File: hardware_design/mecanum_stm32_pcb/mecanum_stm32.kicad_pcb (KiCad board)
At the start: 2 copper layers, 90 x 64 mm, 113 parts, among them J1 BAT 7.4~12.6V, J10 MOTOR A, J11 MOTOR B, J12 MOTOR C, J13 MOTOR D, J2 USB Mini-B, J3 SWD, J4 I2C (MPU6050), J5 SPI IMU, Q1 AO4407A, SW1 RESET, SW2 BOOT0, U1 STM32F405RGT6, U10 DRV8874PWPR, U11 DRV8874PWPR, U12 DRV8874PWPR, U13 DRV8874PWPR, U2 TPS542025 (5V), U3 AMS1117-3.3, U4 CH340C, U5 ADuM1201ARZ, Y1 8MHz 3225 12pF

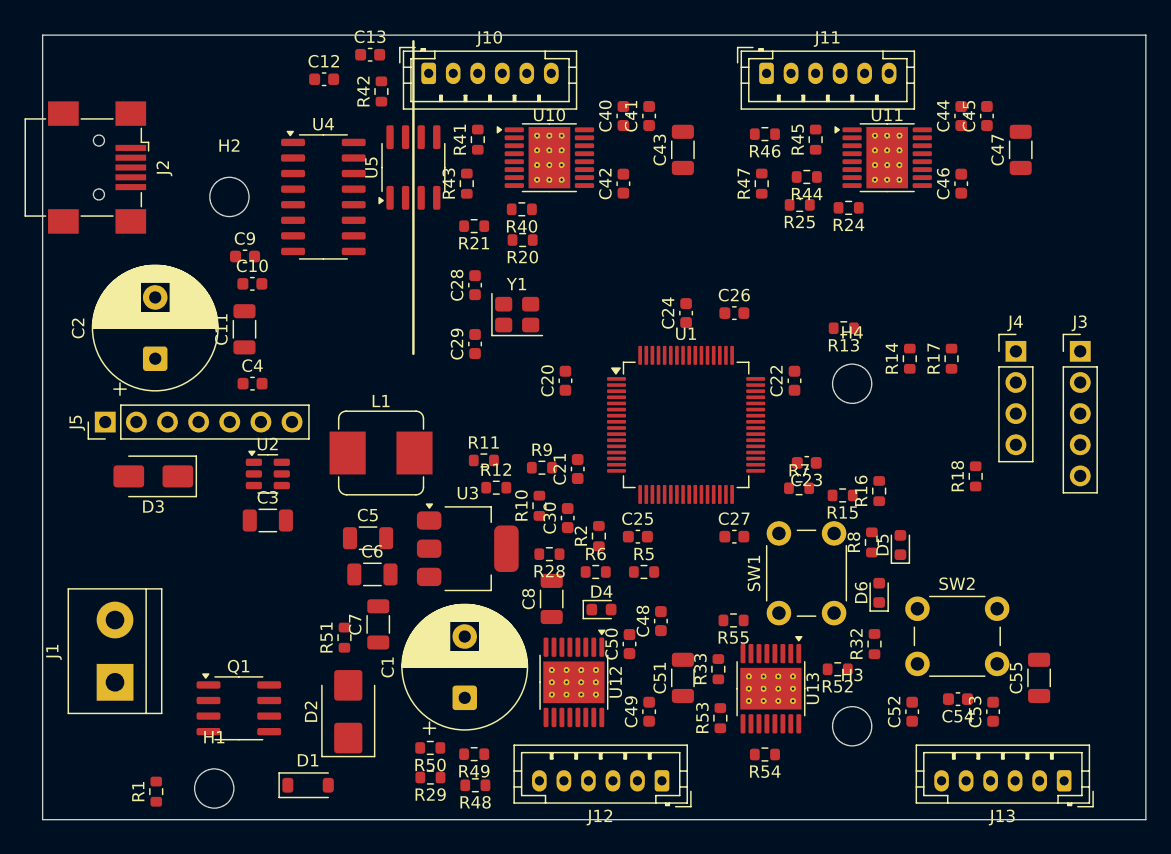
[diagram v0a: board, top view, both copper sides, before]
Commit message: STM32 주행보드 자동배선 완료: 미연결 0·DRC 오류 0, DSN/SES 변환 직접 구현
- route.py: KiCad 9.0.4 ExportSpecctraDSN이 헤드리스에서 멈춰 DSN 쓰기·SES 읽기를 직접 구현,
  Freerouting 2.5.0 연결. 핀에 들어가는 굵기로 배선 후 간격 되는 구간만 0.8/0.6mm로 굵히기,
  양면 GND 동박(USB 칸 GNDU 분리), 고정구멍 둘레 Ø6.5 동박 금지(나사머리가 GNDU를 잇지 않게)
- 넷클래스: Power/Motor/Supply/Default(0.18/0.15mm), 방열 스포크 최소 1
- gen_pcb.py: Mini-B 0.12mm 안쪽, 부품번호 글자 0.8mm
- DRC: 오류 0, 미연결 0, 실크 경고 69

Co-Authored-By: Claude Opus 5.5 <noreply@anthropic.com>
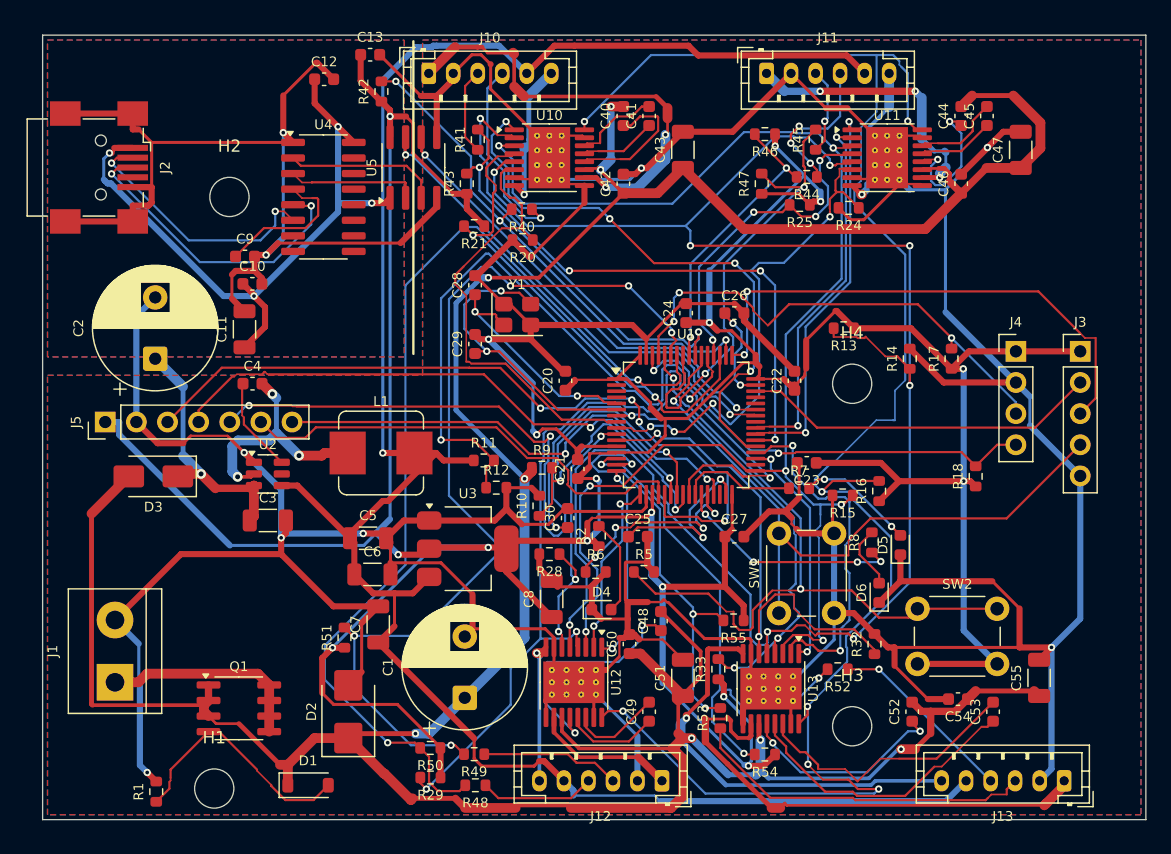
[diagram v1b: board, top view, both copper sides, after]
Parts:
- moved J2 0.16 mm to (4.75, 10.8)
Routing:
- net GND: track 0.00 -> 561.1 mm, vias 0 -> 9
- net 3V3: track 0.00 -> 363.5 mm, vias 0 -> 15
- net VM: track 0.00 -> 283.4 mm, vias 0 -> 8
- net 5V: track 0.00 -> 169.3 mm, vias 0 -> 1
- net VREF: track 0.00 -> 153.6 mm, vias 0 -> 8
- net PMODE: track 0.00 -> 145.9 mm, vias 0 -> 7
- net NSLEEP: track 0.00 -> 121.1 mm, vias 0 -> 7
- net ENC_C_A: track 0.00 -> 83.6 mm, vias 0 -> 2
- net GNDU: track 0.00 -> 80.8 mm, vias 0 -> 2
- net ENC_C_B: track 0.00 -> 77.3 mm, vias 0 -> 5
- net NRST: track 0.00 -> 70.9 mm, vias 0 -> 2
- net V5_SNS: track 0.00 -> 68.8 mm, vias 0 -> 2
- net SPI_SCK: track 0.00 -> 63.5 mm, vias 0 -> 4
- net FLT_C: track 0.00 -> 60.7 mm, vias 0 -> 3
- net SPI_MOSI: track 0.00 -> 60.5 mm, vias 0 -> 3
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- added copper zone on B.Cu, net GND
- added copper zone on F.Cu, net GND
- added copper zone on B.Cu, net GNDU
- added copper zone on F.Cu, net GNDU
